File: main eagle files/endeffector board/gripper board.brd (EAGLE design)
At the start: 63.4 x 147 mm, 92 parts, among them IC1 OPAMP-DUALU, J1 APPPP45_PCB_HORIZ_RIGHT, J10 APPPP45_PCB_HORIZ_RIGHT, J11 APPPP45_PCB_HORIZ_RIGHT, J12 APPPP45_PCB_HORIZ_RIGHT, J13 APPPP45_PCB_HORIZ_RIGHT, J14 APPPP45_PCB_HORIZ_RIGHT, J15 APPPP45_PCB_HORIZ_RIGHT, J16 APPPP45_PCB_HORIZ_RIGHT, J17 APPPP45_PCB_HORIZ_RIGHT, J18 APPPP45_PCB_HORIZ_RIGHT, J2 APPPP45_PCB_HORIZ_RIGHT, J3 APPPP45_PCB_HORIZ_RIGHT, J4 APPPP45_PCB_HORIZ_RIGHT, J5 APPPP45_PCB_HORIZ_RIGHT, J6 APPPP45_PCB_HORIZ_RIGHT, J7 APPPP45_PCB_HORIZ_RIGHT, J8 APPPP45_PCB_HORIZ_RIGHT, J9 APPPP45_PCB_HORIZ_RIGHT, Q1 Q_IRF7437SMD, U1 TIVA-1294, U2 XBEE_802.15.4SMD

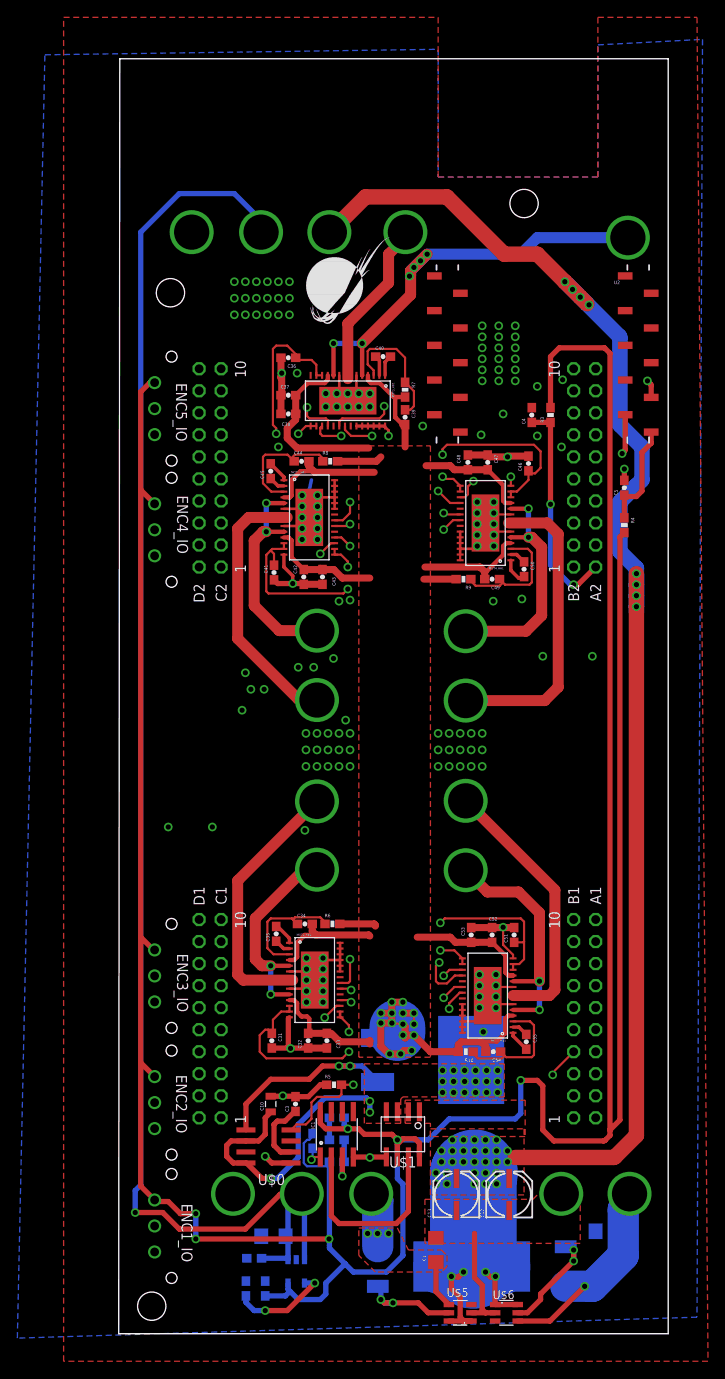
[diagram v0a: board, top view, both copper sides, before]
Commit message: Created branch for endeffector board
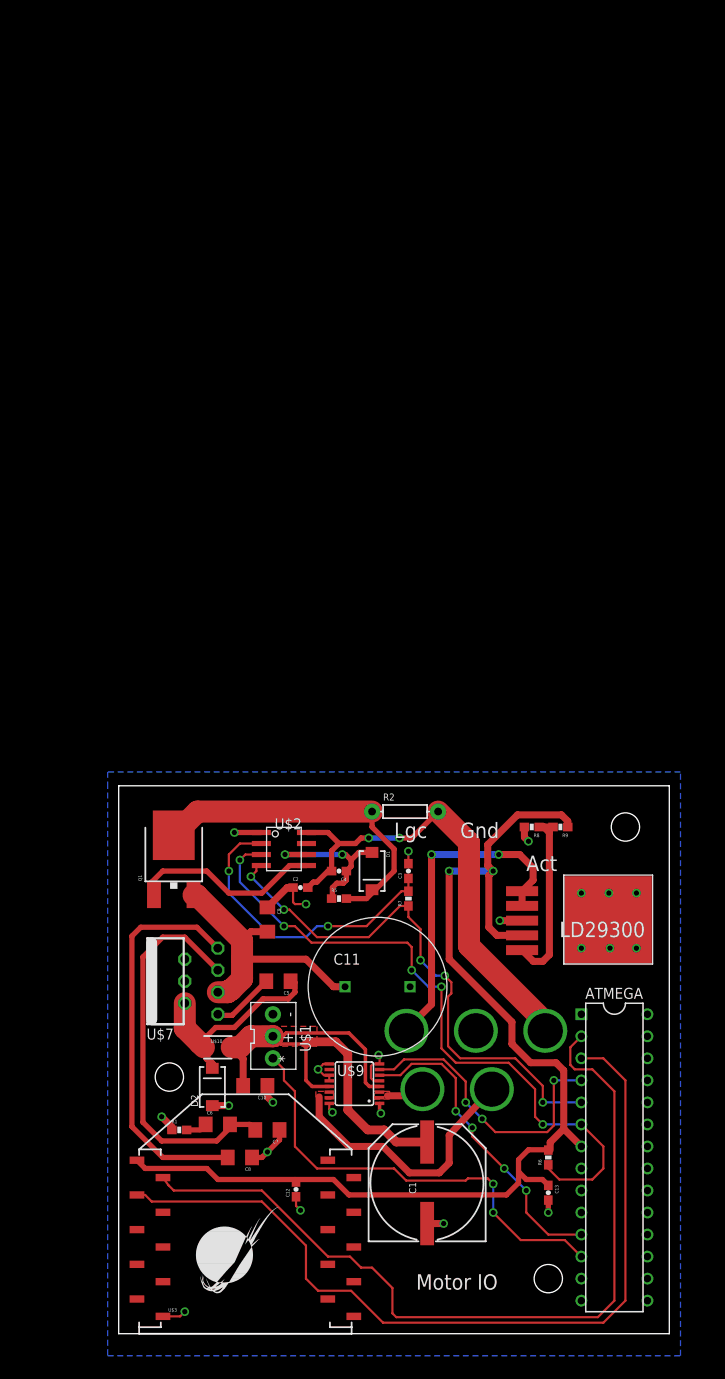
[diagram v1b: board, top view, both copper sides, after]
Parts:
- removed C31, C36, C41, C46, C51: .47uF, SparkFun-Capacitors:0603-CAP
- removed C32, C37, C42, C47, C52: 100uF, SparkFun-Capacitors:0603-CAP
- removed C33, C34, C38, C39, C43, C44, C48, C49, C53, C54: .1uF, SparkFun-Capacitors:0603-CAP
- removed C35, C40, C45, C50, C55: .01uF, SparkFun-Capacitors:0603-CAP
- removed ENC1_IO, ENC2_IO, ENC3_IO, ENC4_IO, ENC5_IO: MF03VERT, MRDT-Connectors:MOLEX0436500328
- removed IC1: OPAMP-DUALU, SparkFun-AnalogIC:SO08
- removed J10, J11, J12, J13, J14, J15, J16, J17, J18, J6, J7, J8, J9: APPPP45_PCB_HORIZ_RIGHT, MRDT-Connectors:APP45_PCB_HORIZ_RIGHT
- removed MOT1_HB1, MOT2_HB1, MOT3_HB1, MOT4_HB1, MOT5_HB1: DRV8829, lin reg:TSSOP28-GROUNDPAD
- removed R10: 1M, SparkFun-Passives:0603-RES
- removed R11: 10k, SparkFun-Passives:0603-RES
- removed R3, R4: 1k, SparkFun-Passives:0603-RES
- removed U$0: LT1910, MRDT-2015-PowerBoard:SO8
- removed U$4: SUD15N15, mine:TO252
- removed U$5, U$6: LM5050, mine:TSOT23-6
- removed U1: TIVA-1294, MRDT-Microcontrollers:TIVA-C-CONNECTED
- removed U2: XBEE_802.15.4SMD, MRDT-Microcontrollers:XBEE_802.15.4_SMD
- added ATMEGA: Q_ATMEGA328P, MRDT-2014-All:DIP28
- added D1: (no value), MRDT-EAGLE-Training:SMA-DIODE
- added D2: DIODE-SCHOTTKY_, SparkFun-DiscreteSemi:SMA-DIODE
- added U$10: 56UH, SparkFun-Capacitors:1210
- added U$7: SANC8050, opamps:TO-220-7
- added U$8: LD29300, mylib1:P2PAK
- added U$9: MAX14871, tssopep:TSSOP-16
- C1: value 2.2uF -> 470uF; device SparkFun-Capacitors:1206 -> SparkFun-Capacitors:PANASONIC_H13
- C10: value 10uF -> 4.7uF; device SparkFun-Capacitors:0805 -> MRDT-EAGLE-Training:1206
- C11: value 2.2uF -> 2200uF; device SparkFun-Capacitors:1206 -> MRDT-2014-All:C_16MM
- C12, C13: value (none) -> 1uF; device SparkFun-Capacitors:PANASONIC_C -> SparkFun-Capacitors:0603-CAP
- C2: value 2.2uF -> 10uF; device SparkFun-Capacitors:1206 -> SparkFun-Capacitors:0603-CAP
- C3: value 1.0uF -> 1uF
- C4: value 0.01uF -> 1uF
- C5: value 0.01uF -> .22uF; device SparkFun-Capacitors:0603-CAP -> MRDT-EAGLE-Training:1206
- C6: value 1.0uF -> 1200pF; device SparkFun-Capacitors:0603-CAP -> MRDT-EAGLE-Training:1206
- C7: value 2.2uF -> 680pF; device SparkFun-Capacitors:0603-CAP -> MRDT-EAGLE-Training:1206
- C8: value 470pF -> 4.7uF; device SparkFun-Capacitors:0603-CAP -> MRDT-EAGLE-Training:1206
- C9: value 2.2uF -> 4.7uF; device SparkFun-Capacitors:0603-CAP -> MRDT-EAGLE-Training:1206
- Q1: value Q_IRF7437SMD -> MOSFET-NCHANNELFDD8780; device MRDT-2015-PowerBoard:D2PACK -> SparkFun-DiscreteSemi:DPAK
- R1: value 6k -> 5100 ohm
- R2: value 4k -> .01; device SparkFun-Passives:0603-RES -> SparkFun-Resistors:AXIAL-0.3
- R5: value 10k -> 10000 ohm
- R6: value 1M -> 5100 ohm
- R7: value 1M -> 2000 ohm
- R8: value 1M -> 1000 ohm
- R9: value 1M -> 3000 ohm
- U$1: value ACS722LL -> SERVO; device lin reg:SOIC8 -> MRDT-2015-General:SERVO_JACK
- U$2: value MIC5219-3.3YM5 -> LT1910; device lin reg:SOT-23-5 -> mylib1:SOIC8
- U$3: value SUD15N15 -> XBEE-1B3; device mine:TO252 -> SparkFun-RF:XBEE-SMD
- moved H1 121.7 mm to (49.5, 6.35)
- moved LOGO1 112.5 mm to (8.89, 3.81)
- moved H3 108.7 mm to (5.84, 29.6)
- moved J4 88.9 mm to (39.0, 0.00), turned to 90 degrees
- moved J5 86.7 mm to (47.0, 0.00), turned to 90 degrees
- moved J1 77.8 mm to (37.2, 63.1), turned to 270 degrees
- moved H2 77.7 mm to (58.4, 58.4)
- moved J3 76.2 mm to (45.2, 63.1), turned to 270 degrees
- moved J2 75.3 mm to (29.2, 63.1), turned to 270 degrees
- moved C5 69.5 mm to (18.4, 40.6), turned to 180 degrees
- moved R7 58.7 mm to (33.4, 50.2), turned to 90 degrees
- moved C4 57.1 mm to (25.4, 53.3), turned to 180 degrees
- moved R8 48.1 mm to (47.6, 58.4), turned to 180 degrees
- moved U$2 47.9 mm to (19.1, 55.9), flipped to the top, turned to 0 degrees
- moved R2 41.1 mm to (33.0, 60.2), flipped to the top, turned to 0 degrees
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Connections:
- removed net $N3: C10.1, Q1.TAB, U$0.6, U$0.8, U$1.3, U$1.4
- removed net A: C5.1, R4.1, U2.1
- removed net ACT_PWR_UNGUARDED: C1.1, J3.P$1, U$3.2, U$5.4
- removed net DUAL_PWR: C12.+, C13.+, J16.P$1, U$1.1, U$1.2, U$3.3, U$4.3, U$5.1, U$5.6, U$6.1, U$6.6
- removed net ENC1_PWM_OUT: ENC1_IO.P$2, U1.PD2
- removed net ENC2_PWM_OUT: ENC2_IO.P$2, U1.PA4
- removed net ENC3_PWM_OUT: ENC3_IO.P$2, U1.PD4
- removed net ENC4_PWM_OUT: ENC4_IO.P$2, U1.PM4
- removed net ENC5_PWM_OUT: ENC5_IO.P$2, U1.PB2
- removed net EXTRA_PWR: C11.1, J18.P$1, U$4.2, U$6.4
- removed net HB_3.3_OUTPUT5: C31.1, MOT1_HB1.12, MOT1_HB1.13, MOT1_HB1.15, MOT1_HB1.16
- removed net HB_3.3_OUTPUT6: C36.1, MOT3_HB1.12, MOT3_HB1.13, MOT3_HB1.15, MOT3_HB1.16
- removed net HB_3.3_OUTPUT7: C41.1, MOT2_HB1.12, MOT2_HB1.13, MOT2_HB1.15, MOT2_HB1.16
- removed net HB_3.3_OUTPUT8: C46.1, MOT4_HB1.12, MOT4_HB1.13, MOT4_HB1.15, MOT4_HB1.16
- removed net HB_3.3_OUTPUT9: C51.1, MOT5_HB1.12, MOT5_HB1.13, MOT5_HB1.15, MOT5_HB1.16
- removed net LOG_PWR_12V: C2.2, C6.1, J15.P$1, J2.P$1, U$2.1, U$2.3
- removed net LOG_PWR_3.3V: C7.1, C9.1, ENC1_IO.P$1, ENC2_IO.P$1, ENC3_IO.P$1, ENC4_IO.P$1, ENC5_IO.P$1, IC1.8, R11.2, R2.1, R3.2, R4.2, U$1.6, U$1.8, U$2.5
- removed net MAIN_PWR_SWITCH_CTL: R5.1, U$0.4, U1.PM7
- removed net MAIN_PWR_SWITCH_NFAULT: IC1.1, R11.1, U1.PP5
- removed net MOT1_1: J10.P$1, MOT1_HB1.10, MOT1_HB1.5
- removed net MOT1_2: J11.P$1, MOT1_HB1.7, MOT1_HB1.8
- removed net MOT1_NFAULT: MOT1_HB1.18, U1.PE0
- removed net MOT1_NSLEEP: MOT1_HB1.17, U1.PE1
- removed net MOT1_PHASE: MOT1_HB1.20, U1.PE2
- removed net MOT1_PWM: MOT1_HB1.21, U1.PF1
- removed net MOT2_1: J4.P$1, MOT2_HB1.10, MOT2_HB1.5
- removed net MOT2_2: J5.P$1, MOT2_HB1.7, MOT2_HB1.8
- removed net MOT2_NFAULT: MOT2_HB1.18, U1.PE3
- removed net MOT2_NSLEEP: MOT2_HB1.17, U1.PD7
- removed net MOT2_PHASE: MOT2_HB1.20, U1.PM5
- removed net MOT2_PWM: MOT2_HB1.21, U1.PF2
- removed net MOT3_1: J12.P$1, MOT3_HB1.10, MOT3_HB1.5
- removed net MOT3_2: J13.P$1, MOT3_HB1.7, MOT3_HB1.8
- removed net MOT3_NFAULT: MOT3_HB1.18, U1.PB4
- removed net MOT3_NSLEEP: MOT3_HB1.17, U1.PB5
- removed net MOT3_PHASE: MOT3_HB1.20, U1.PK2
- removed net MOT3_PWM: MOT3_HB1.21, U1.PF3
- removed net MOT4_1: J6.P$1, MOT4_HB1.10, MOT4_HB1.5
- removed net MOT4_2: J7.P$1, MOT4_HB1.7, MOT4_HB1.8
- removed net MOT4_NFAULT: MOT4_HB1.18, U1.PK3
- removed net MOT4_NSLEEP: MOT4_HB1.17, U1.PA5
- removed net MOT4_PHASE: MOT4_HB1.20, U1.PP4
- removed net MOT4_PWM: MOT4_HB1.21, U1.PK4
- removed net MOT5_1: J8.P$1, MOT5_HB1.10, MOT5_HB1.5
- removed net MOT5_2: J9.P$1, MOT5_HB1.7, MOT5_HB1.8
- removed net MOT5_NFAULT: MOT5_HB1.18, U1.PH1
- removed net MOT5_NSLEEP: MOT5_HB1.17, U1.PK6
- removed net MOT5_PHASE: MOT5_HB1.20, U1.PK7
- removed net MOT5_PWM: MOT5_HB1.21, U1.PK5
- removed net MTR_PWR: C32.2, C33.2, C34.2, C37.2, C38.2, C39.2, C42.2, C43.2, C44.2, C47.2, C48.2, C49.2, C52.2, C53.2, C54.2, MOT1_HB1.11, MOT1_HB1.4, MOT2_HB1.11, MOT2_HB1.4, MOT3_HB1.11, MOT3_HB1.4, MOT4_HB1.11, MOT4_HB1.4, MOT5_HB1.11, MOT5_HB1.4, Q1.2, R10.2, R6.2, R7.2, R8.2, R9.2
- removed net N$17: C34.1, MOT1_HB1.3, R6.1
- removed net N$18: C35.2, MOT1_HB1.1
- removed net N$19: C35.1, MOT1_HB1.2
- removed net N$2: C8.1, U$2.4
- removed net N$20: C39.1, MOT3_HB1.3, R7.1
- removed net N$21: C40.2, MOT3_HB1.1
- removed net N$22: C40.1, MOT3_HB1.2
- removed net N$23: C44.1, MOT2_HB1.3, R8.1
- removed net N$24: C45.2, MOT2_HB1.1
- removed net N$25: C45.1, MOT2_HB1.2
- removed net N$26: C49.1, MOT4_HB1.3, R9.1
- removed net N$27: C50.2, MOT4_HB1.1
- removed net N$28: C50.1, MOT4_HB1.2
- removed net N$29: C54.1, MOT5_HB1.3, R10.1
- removed net N$30: C55.2, MOT5_HB1.1
- removed net N$31: C55.1, MOT5_HB1.2
- removed net RX7_XBEE_OUT: U1.PC4, U2.2
- removed net SF: C4.2, R3.1, U1.+3V3_1, U1.+3V3_2
- removed net TX7_XBEE_IN: U1.PC5, U2.3
- new net 12VLGC: J2.P$1, U$8.1, U$8.2
- new net 12VMTR: C11.+, C9.2, Q1.3, U$7.3
- new net 5VIN: ATMEGA.7, C12.2, C13.1, R6.2, R9.1, U$3.1, U$8.4
- new net 5VMTR: C1.+, C10.2, U$1.VCC, U$10.2, U$9.13, U$9.4
- new net ACTPWR: C2.2, C4.2, J3.P$1, R2.P$2, U$2.8
- new net ATMEGA2XBEE: ATMEGA.3, U$3.3
- new net FAULT: ATMEGA.6, R6.1, U$2.3
- new net MICROCNTRL: ATMEGA.5, R7.1, U$2.4
- new net MTR1_1: J4.P$1, U$9.2, U$9.3
- new net MTR1_2: J5.P$1, U$9.14, U$9.15
- new net MTR1_DIR: ATMEGA.4, U$9.7
- new net MTR1_PWM: ATMEGA.11, U$9.6
- new net N$10: C6.2, C7.2, U$7.5
- new net N$12: C5.2, U$7.1
- new net N$6: C4.1, D1.A, R5.1, U$2.6
- new net N$9: D1.C, Q1.4, R2.P$1, R5.2
- new net SERVOIN: ATMEGA.12, U$1.SIGNAL
- new net XBEE2ATMEGA: ATMEGA.2, U$3.2
- net GND: now also ATMEGA.22, ATMEGA.8, C1.-, C10.1, C11.GND, C12.1, C13.2, C7.1, C8.1, C9.1, D2.A, R1.1, R8.2, U$1.GND, U$2.1, U$3.10, U$7.4, U$8.3, U$8.P$1, U$9.1, U$9.11, U$9.12, U$9.16, U$9.5, U$9.8, U$9.9; no longer C1.2, C10.2, C11.2, C12.-, C13.-, C31.2, C32.1, C33.1, C36.2, C37.1, C38.1, C4.1, C41.2, C42.1, C43.1, C46.2, C47.1, C48.1, C5.2, C51.2, C52.1, C53.1, C6.2, C7.2, C8.2, C9.2, ENC1_IO.P$3, ENC2_IO.P$3, ENC3_IO.P$3, ENC4_IO.P$3, ENC5_IO.P$3, IC1.4, J14.P$1, J17.P$1, MOT1_HB1.14, MOT1_HB1.23, MOT1_HB1.24, MOT1_HB1.25, MOT1_HB1.26, MOT1_HB1.27, MOT1_HB1.28, MOT1_HB1.29, MOT1_HB1.6, MOT1_HB1.9, MOT2_HB1.14, MOT2_HB1.23, MOT2_HB1.24, MOT2_HB1.25, MOT2_HB1.26, MOT2_HB1.27, MOT2_HB1.28, MOT2_HB1.29, MOT2_HB1.6, MOT2_HB1.9, MOT3_HB1.14, MOT3_HB1.23, MOT3_HB1.24, MOT3_HB1.25, MOT3_HB1.26, MOT3_HB1.27, MOT3_HB1.28, MOT3_HB1.29, MOT3_HB1.6, MOT3_HB1.9, MOT4_HB1.14, MOT4_HB1.23, MOT4_HB1.24, MOT4_HB1.25, MOT4_HB1.26, MOT4_HB1.27, MOT4_HB1.28, MOT4_HB1.29, MOT4_HB1.6, MOT4_HB1.9, MOT5_HB1.14, MOT5_HB1.23, MOT5_HB1.24, MOT5_HB1.25, MOT5_HB1.26, MOT5_HB1.27, MOT5_HB1.28, MOT5_HB1.29, MOT5_HB1.6, MOT5_HB1.9, R1.2, R5.2, U$0.1, U$1.5, U$2.2, U$5.2, U$6.2, U1.GND_1, U1.GND_2, U1.GND_3, U1.GND_4, U2.10
- net N$1: now also R7.2, U$2.2; no longer U$0.2
- net N$11: now also C5.1, D2.C, U$10.1, U$7.2, U$7.6; no longer U$4.1, U$6.5
- net N$3: now also R8.1, R9.2, U$8.5; no longer Q1.1, U$0.5
- net N$5: now also C6.1, R1.2; no longer IC1.2, U$1.7
- net N$7: now also Q1.1, U$2.5; no longer IC1.3, R1.1, R2.2
- net N$8: now also C8.2, U$7.7; no longer U$3.1, U$5.5
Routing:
- net LOG_PWR_3.3V: track 408.6 -> 0.00 mm, vias 6 -> 0
- net DUAL_PWR: track 204.2 -> 0.00 mm, vias 41 -> 0
- net MTR_PWR: track 185.1 -> 0.00 mm, vias 15 -> 0
- net ENC1_PWM_OUT: track 175.8 -> 0.00 mm, vias 6 -> 0
- net LOG_PWR_12V: track 172.8 -> 0.00 mm, vias 1 -> 0
- net ENC2_PWM_OUT: track 149.3 -> 0.00 mm, vias 4 -> 0
- net 5VIN: track 0.00 -> 131.3 mm, vias 0 -> 2
- net MOT5_PWM: track 122.9 -> 0.00 mm, vias 1 -> 0
- net ENC5_PWM_OUT: track 113.0 -> 0.00 mm, vias 2 -> 0
- net ENC3_PWM_OUT: track 110.0 -> 0.00 mm, vias 4 -> 0
- net ENC4_PWM_OUT: track 105.7 -> 0.00 mm
- net MAIN_PWR_SWITCH_CTL: track 99.4 -> 0.00 mm, vias 1 -> 0
- net MOT3_PWM: track 97.7 -> 0.00 mm, vias 4 -> 0
- net ATMEGA2XBEE: track 0.00 -> 97.2 mm
- net XBEE2ATMEGA: track 0.00 -> 95.6 mm
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- added copper zone on layer 1, net 5VMTR
- added copper zone on layer 1, net MTR1_1
- added copper zone on layer 1, net MTR1_2
- removed copper zone on layer 1, net $N3
- removed copper zone on layer 1, net ACT_PWR_UNGUARDED
- removed copper zone on layer 1, net DUAL_PWR
- removed copper zone on layer 1, net GND
- removed copper zone on layer 1, net MTR_PWR
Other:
- board size 63.4 x 147 mm -> 63.5 x 63.2 mm
- board text added: "Act"
- board text added: "LD29300"
- board text added: "Lgc"
- board text added: "Motor IO"
- board text removed: "MRDT 16-17 Arm board V1 Drue Satterfield Rove so ******* hard you won't even believe it"
- board text removed: "Mot 1"
- board text removed: "Mot 2"
- board text removed: "Mot 3_1"
- board text removed: "Mot 3_2"
- board text removed: "Mot 4"
- board text removed: "Mot 5"
- board text removed: "Power OUTPUT"
- board text removed: "act"
- board text removed: "act pwr"
- board text removed: "extra"
- board text removed: "gnd"
- board text removed: "lgc pwr"
- board text removed: "logic"
- board text removed: "power INPUT"
